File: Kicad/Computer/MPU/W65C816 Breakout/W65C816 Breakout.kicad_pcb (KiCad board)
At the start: 2 copper layers, 26.7 x 90.2 mm, 47 parts, among them IC1 74ALVC164245DGG,11, IC10 SN74LVC1G332DCKRG4, IC12 SN74LVC1G332DCKRG4, IC13 SN74LVC1G332DCKRG4, IC14 SN74LVC1G332DCKRG4, IC15 74LVC2G32DP,125, IC17 74LVC2G08DP-Q100H, IC18 74LVC2G86DP,125, IC19 74LVC125APW-Q100J, IC2 W65C816S6TQG-14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

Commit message: Updated W65C816 Breakout to include Schmitt triggers and resistors on the clock and reset signals.
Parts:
- added IC7: 74LVC1G17GV,125, SamacSys_Parts:SOT95P275X110-5N, F.Cu at (102.9, 88.4)
- added R3: 150Ω, SamacSys_Parts:R_0805, B.Cu at (96.4, 126.4)
- added R4: 150Ω, SamacSys_Parts:R_0805, B.Cu at (103.9, 126.4)
- moved R1 0.65 mm to (105.2, 114.0)
- moved IC8 0.25 mm to (104.4, 83.6)
- moved C18 0.13 mm to (105.5, 83.7)
- turned R2 to 180 degrees
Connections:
- IC1 pad 22: /W65C816 Breakout Board/~{RES}_{5V} -> Net-(IC1C-2B6)
- IC1 pad 23: /W65C816 Breakout Board/PHI2_{5V} -> Net-(IC1C-2B7)
- IC1 pad 27: /W65C816 Breakout Board/~{Reset} -> /W65C816 Breakout Board/~{Reset Sharp}
- IC6 pad 10: /W65C816 Breakout Board/~{Reset} -> /W65C816 Breakout Board/~{Reset Sharp}
- IC6 pad 4: /W65C816 Breakout Board/~{Reset} -> /W65C816 Breakout Board/~{Reset Sharp}
- IC9 pad 13: /W65C816 Breakout Board/~{Reset} -> /W65C816 Breakout Board/~{Reset Sharp}
- R2 pad 1: /W65C816 Breakout Board/BE -> /W65C816 Breakout Board/3.3V
- R2 pad 2: /W65C816 Breakout Board/3.3V -> /W65C816 Breakout Board/BE
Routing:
- net /W65C816 Breakout Board/~{Reset Sharp}: track 0.00 -> 83.1 mm, vias 0 -> 4
- net /W65C816 Breakout Board/GND: track 586.2 -> 621.6 mm, vias 47 -> 50
- net /W65C816 Breakout Board/~{Reset}: track 86.3 -> 52.4 mm, vias 3 -> 2
- net /W65C816 Breakout Board/~{RES}_{5V}: track 23.6 -> 12.6 mm, vias 2 -> 1
- net Net-(IC1C-2B6): track 0.00 -> 9.65 mm, vias 0 -> 1
- net /W65C816 Breakout Board/PHI2_{5V}: track 79.1 -> 73.0 mm, vias 6 -> 5
- net Net-(IC1C-2B7): track 0.00 -> 4.74 mm, vias 0 -> 1
- net /W65C816 Breakout Board/PHI2: track 67.9 -> 64.6 mm
- net /W65C816 Breakout Board/3.3V: track 216.0 -> 213.7 mm
- net /W65C816 Breakout Board/VPA: track 57.6 -> 59.5 mm, vias 4 -> 3
- net /W65C816 Breakout Board/FET ~{OE}: track 62.6 -> 64.0 mm
- net /W65C816 Breakout Board/~{NMI}: track 12.6 -> 13.9 mm
- net /W65C816 Breakout Board/~{RD}: track 14.6 -> 13.7 mm
- net /W65C816 Breakout Board/~{PHI2}: track 98.6 -> 99.5 mm
- net /W65C816 Breakout Board/A0_{CHANGE}: track 11.4 -> 10.6 mm
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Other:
- board text added: "W65C816 Breakout V1"
- board text removed: "W65C816 Breakout V0"

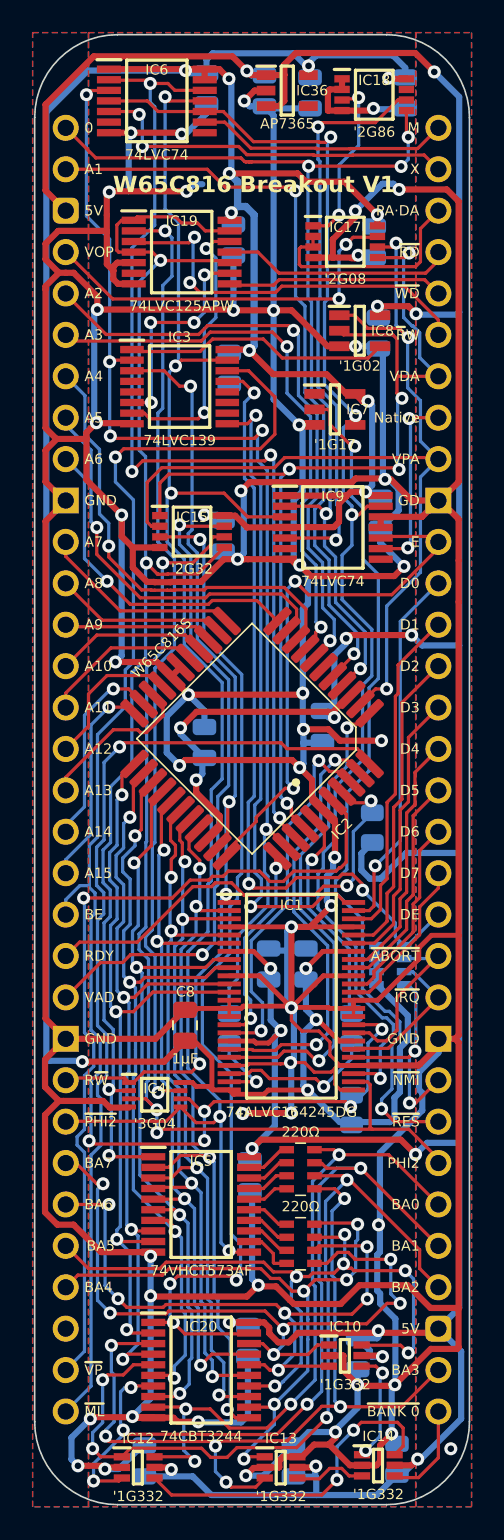
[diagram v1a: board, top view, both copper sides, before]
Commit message: Changed clock smoothing resistor to 20ohms.
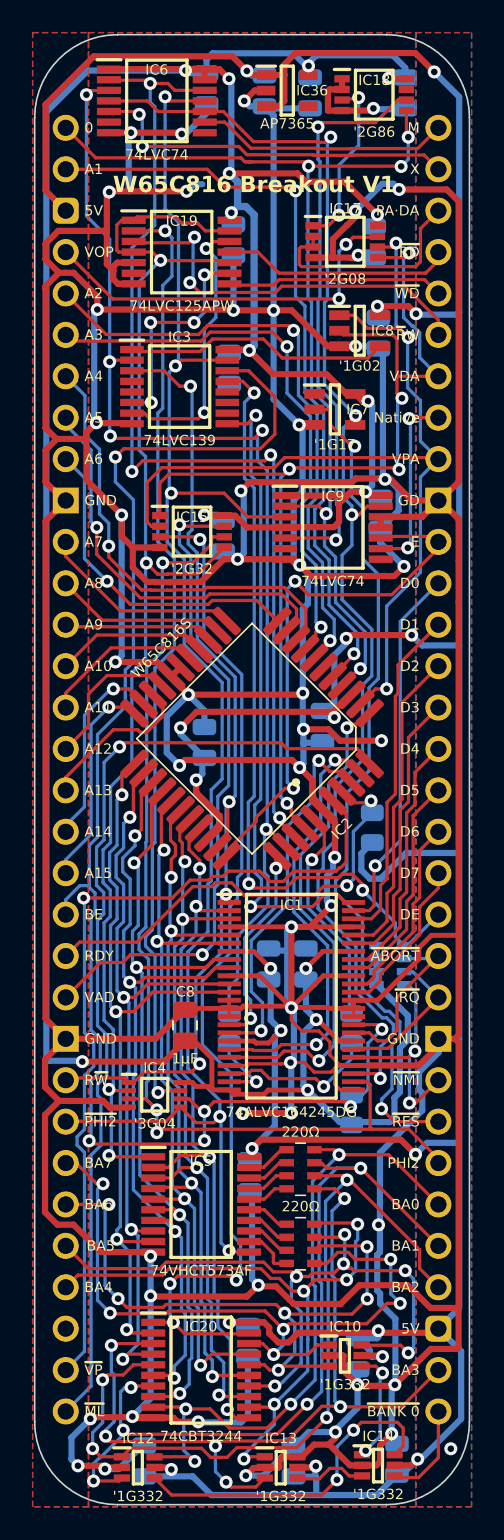
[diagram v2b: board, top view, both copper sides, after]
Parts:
- R3, R4: value 150Ω -> 20Ω
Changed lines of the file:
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@@
       (net 72 "/W65C816 Breakout Board/~{PHI2}") (pinfunction "LE") (pintype "input"))
     (pad "12" smd rect (at 2.938 2.275 90) (size 0.45 1.475) (layers "F.Cu" "F.Paste" "F.Mask")
-      (net 75 "/W65C816 Breakout Board/D7_{VHC}") (pinfunction "Q7") (pintype "output"))
+      (net 75 "/W65C816 Breakout Board/D7_{VHC}") (pinfunction "Q7") (pintype "tri_state"))
     (pad "13" smd rect (at 2.938 1.625 90) (size 0.45 1.475) (layers "F.Cu" "F.Paste" "F.Mask")
-      (net 76 "/W65C816 Breakout Board/D6_{VHC}") (pinfunction "Q6") (pintype "output"))
+      (net 76 "/W65C816 Breakout Board/D6_{VHC}") (pinfunction "Q6") (pintype "tri_state"))
     (pad "14" smd rect (at 2.938 0.975 90) (size 0.45 1.475) (layers "F.Cu" "F.Paste" "F.Mask")
-      (net 77 "/W65C816 Breakout Board/D5_{VHC}") (pinfunction "Q5") (pintype "output"))
+      (net 77 "/W65C816 Breakout Board/D5_{VHC}") (pinfunction "Q5") (pintype "tri_state"))
     (pad "15" smd rect (at 2.938 0.325 90) (size 0.45 1.475) (layers "F.Cu" "F.Paste" "F.Mask")
-      (net 78 "/W65C816 Breakout Board/D4_{VHC}") (pinfunction "Q4") (pintype "output"))
+      (net 78 "/W65C816 Breakout Board/D4_{VHC}") (pinfunction "Q4") (pintype "tri_state"))
     (pad "16" smd rect (at 2.938 -0.325 90) (size 0.45 1.475) (layers "F.Cu" "F.Paste" "F.Mask")
-      (net 79 "/W65C816 Breakout Board/D3_{VHC}") (pinfunction "Q3") (pintype "output"))
+      (net 79 "/W65C816 Breakout Board/D3_{VHC}") (pinfunction "Q3") (pintype "tri_state"))
     (pad "17" smd rect (at 2.938 -0.975 90) (size 0.45 1.475) (layers "F.Cu" "F.Paste" "F.Mask")
-      (net 80 "/W65C816 Breakout Board/D2_{VHC}") (pinfunction "Q2") (pintype "output"))
+      (net 80 "/W65C816 Breakout Board/D2_{VHC}") (pinfunction "Q2") (pintype "tri_state"))
     (pad "18" smd rect (at 2.938 -1.625 90) (size 0.45 1.475) (layers "F.Cu" "F.Paste" "F.Mask")
-      (net 81 "/W65C816 Breakout Board/D1_{VHC}") (pinfunction "Q1") (pintype "output"))
+      (net 81 "/W65C816 Breakout Board/D1_{VHC}") (pinfunction "Q1") (pintype "tri_state"))
     (pad "19" smd rect (at 2.938 -2.275 90) (size 0.45 1.475) (layers "F.Cu" "F.Paste" "F.Mask")
-      (net 82 "/W65C816 Breakout Board/D0_{VHC}") (pinfunction "Q0") (pintype "output"))
+      (net 82 "/W65C816 Breakout Board/D0_{VHC}") (pinfunction "Q0") (pintype "tri_state"))
     (pad "20" smd rect (at 2.938 -2.925 90) (size 0.45 1.475) (layers "F.Cu" "F.Paste" "F.Mask")
       (net 13 "/W65C816 Breakout Board/5V") (pinfunction "5V") (pintype "passive"))
@@
     (property "ki_description" "TRIPLE INVERTER GATE")
     (attr smd)
-    (fp_text reference "IC4" (at 0 -0.381) (layer "F.SilkS")
+    (fp_text reference "IC4" (at 0 -1.651) (layer "F.SilkS")
         (effects (font (size 0.635 0.635) (thickness 0.15)))
     )
@@
     (property "ki_description" "74LVC2G08-Q100 - Dual 2-input AND gate@en-us")
     (attr smd)
-    (fp_text reference "IC17" (at 0 -0.889) (layer "F.SilkS")
+    (fp_text reference "IC17" (at 0 -2.032) (layer "F.SilkS")
         (effects (font (size 0.635 0.635) (thickness 0.15)))
     )
@@
         (effects (font (size 0.635 0.635) (thickness 0.15)) (justify mirror))
     )
-    (fp_text value "150Ω" (at 0 -2.032) (layer "B.SilkS")
+    (fp_text value "20Ω" (at 0 -2.032) (layer "B.SilkS")
         (effects (font (size 0.635 0.635) (thickness 0.15)) (justify mirror))
     )
@@
         (effects (font (size 0.635 0.635) (thickness 0.15)) (justify mirror))
     )
-    (fp_text value "150Ω" (at 0 -2.032) (layer "B.SilkS")
-        (effects (font (size 0.635 0.635) (thickness 0.15)) (justify mirror))
-    )
+    (fp_text value "20Ω" (at 0 -2.032) (layer "B.SilkS")
+        (effects (font (size 0.635 0.635) (thickness 0.15)) (justify mirror))
+    )

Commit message: Added Main Memory Select and W65C816 Debug Display.
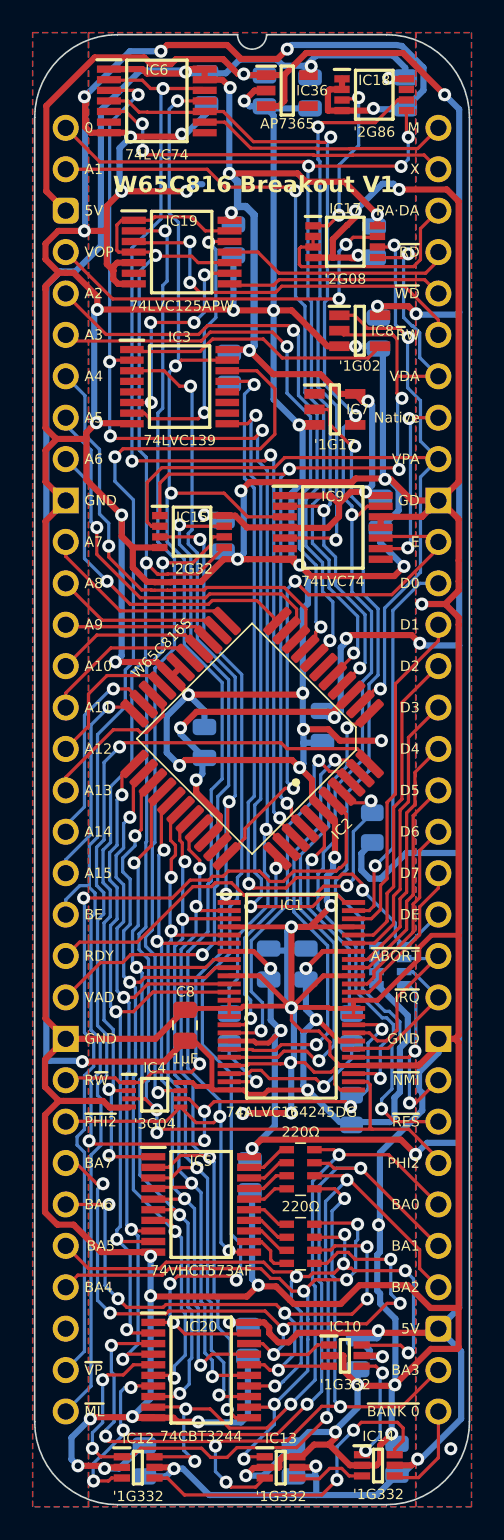
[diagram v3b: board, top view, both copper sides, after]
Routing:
- net /W65C816 Breakout Board/GND: track 621.6 -> 661.4 mm, vias 50 -> 55
- net /W65C816 Breakout Board/3.3V: track 213.7 -> 210.8 mm
- net /W65C816 Breakout Board/MX: track 63.7 -> 62.4 mm
- net /W65C816 Breakout Board/~{PHI2}: track 99.5 -> 98.4 mm
- net /W65C816 Breakout Board/~{R}W: track 23.7 -> 23.0 mm
- net /W65C816 Breakout Board/D0: track 22.8 -> 23.5 mm
- net /W65C816 Breakout Board/PHI2_{5V}: track 73.0 -> 73.6 mm
- net /W65C816 Breakout Board/~{Reset Sharp}: track 83.1 -> 82.6 mm
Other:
- outline, holes or cut-outs redrawn

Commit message: Updated some MPU boards with new DIP footprint.
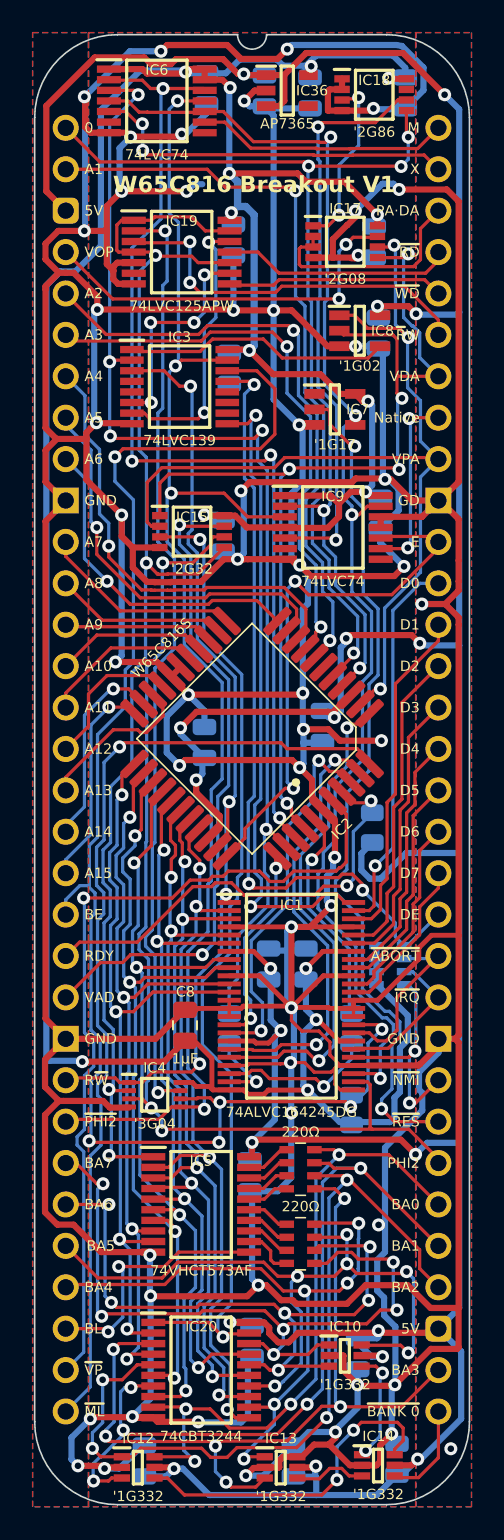
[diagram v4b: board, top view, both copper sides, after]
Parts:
- moved C9 0.25 mm to (97.8, 145.5)
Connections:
- IC5 pad 11: /W65C816 Breakout Board/~{PHI2} -> /W65C816 Breakout Board/Bank Latch
- J7 pad 30: unconnected-(J7-Pin_30-Pad30) -> /W65C816 Breakout Board/Bank Latch
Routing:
- net /W65C816 Breakout Board/Bank Latch: track 0.00 -> 15.5 mm, vias 0 -> 2
- net /W65C816 Breakout Board/~{PHI2}: track 98.4 -> 86.2 mm, vias 5 -> 4
- net /W65C816 Breakout Board/GND: track 661.4 -> 665.1 mm, vias 55 -> 54
- net /W65C816 Breakout Board/FET ~{OE}: track 64.0 -> 61.0 mm, vias 4 -> 2
- net /W65C816 Breakout Board/BE: track 91.2 -> 92.2 mm
- net /W65C816 Breakout Board/D3_{65}: track 45.0 -> 45.9 mm
- net /W65C816 Breakout Board/BA6: track 40.9 -> 41.8 mm
- net /W65C816 Breakout Board/PHI2: track 64.6 -> 63.8 mm
- net /W65C816 Breakout Board/BA5: track 43.8 -> 44.6 mm
- net /W65C816 Breakout Board/D2_{65}: track 43.9 -> 44.5 mm
- net /W65C816 Breakout Board/D1_{65}: track 44.2 -> 44.7 mm
- net /W65C816 Breakout Board/BA7: track 44.9 -> 45.4 mm
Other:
- board text added: "BL"

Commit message: Trying out the Paneliser again.
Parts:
- removed IC4: SN74LVC3G04DCUR, SamacSys_Parts:SOP50P310X90-8N
- added IC11: 74LVC2G04GW-Q100H, SamacSys_Parts:SOP65P210X110-6N, F.Cu at (91.9, 131.1)
- moved IC8 0.51 mm to (103.9, 83.6)
- moved C11 0.38 mm to (104.9, 78.1)
- moved C18 0.38 mm to (105.2, 83.7)
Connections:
- IC19 pad 1: /W65C816 Breakout Board/~{BE} -> /W65C816 Breakout Board/GND
- IC19 pad 2: /W65C816 Breakout Board/RW_{PART} -> /W65C816 Breakout Board/GND
- IC19 pad 3: /W65C816 Breakout Board/~{R}W -> unconnected-(IC19-1Y-Pad3)
- IC19 pad 4: /W65C816 Breakout Board/~{BE} -> /W65C816 Breakout Board/GND
- IC3 pad 15: /W65C816 Breakout Board/~{PHI2} -> /W65C816 Breakout Board/~{Trans Output}
- J7 pad 58: /W65C816 Breakout Board/VDA -> /W65C816 Breakout Board/~{Trans Output}
- J7 pad 59: /W65C816 Breakout Board/~{R}W -> /W65C816 Breakout Board/VDA
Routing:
- net /W65C816 Breakout Board/RW_{PART}: track 58.0 -> 0.00 mm, vias 2 -> 0
- net /W65C816 Breakout Board/~{R}W: track 23.0 -> 0.00 mm, vias 2 -> 0
- net /W65C816 Breakout Board/~{Trans Output}: track 0.00 -> 13.4 mm
- net /W65C816 Breakout Board/GND: track 665.1 -> 673.7 mm
- net /W65C816 Breakout Board/3.3V: track 210.8 -> 217.9 mm
- net /W65C816 Breakout Board/~{BE}: track 83.7 -> 78.2 mm
- net /W65C816 Breakout Board/~{PHI2}: track 86.2 -> 82.9 mm, vias 4 -> 3
- net /W65C816 Breakout Board/VDA: track 65.1 -> 61.7 mm
- net /W65C816 Breakout Board/5V: track 251.9 -> 253.4 mm
- net /W65C816 Breakout Board/~{WD}: track 13.2 -> 12.2 mm
- net /W65C816 Breakout Board/VPA: track 59.1 -> 59.8 mm
- net /W65C816 Breakout Board/BE: track 92.2 -> 92.8 mm
- net /W65C816 Breakout Board/R~{W}: track 58.9 -> 59.5 mm
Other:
- board text added: "~{TOE}"
- board text removed: "~{R}W"
